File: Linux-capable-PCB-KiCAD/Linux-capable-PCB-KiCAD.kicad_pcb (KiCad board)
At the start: 4 copper layers, 167 parts, among them J1 UART_CONN, J2 GPIO_CONN, J3 USB_A, J4 USB_A, J5 Micro_SD_Card_Det, J6 MIC_DIFF_IN, J7 Barrel_Jack, U1 A33, U10 TPS62130, U11 AP131-25, U12 TPS62130, U13 TPS62130, U2 MMA8425Q_Gsensor, U3 SRV05-4, U4 MIPI_DSI_Raspberry, U5 SRV05-4, U6 SRV05-4, U7 ESP8089, U8 HTQ4G63AFR-PCB, U9 TPS62130, Y1 24MHz, Y2 32.768kHz, Y3 26 MHz

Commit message: clearence needs to be resolved
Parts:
- moved U8 42.0 mm to (172.7, 68.6), turned to 90 degrees
- moved U7 31.9 mm to (130.8, 54.6)
- moved J5 15.3 mm to (143.5, 50.8)
- moved U1 7.77 mm to (152.4, 78.7), turned to 180 degrees
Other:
- net class Outer_small added: clearance 0.1, trace_width 0.1, via_dia 0.4, via_drill 0.2
- net class Power added: clearance 0.2, trace_width 1, via_dia 0.8, via_drill 0.6
- rule trace_min: 0.2 -> 0.09
- rule via_min_drill: 0.3 -> 0.2

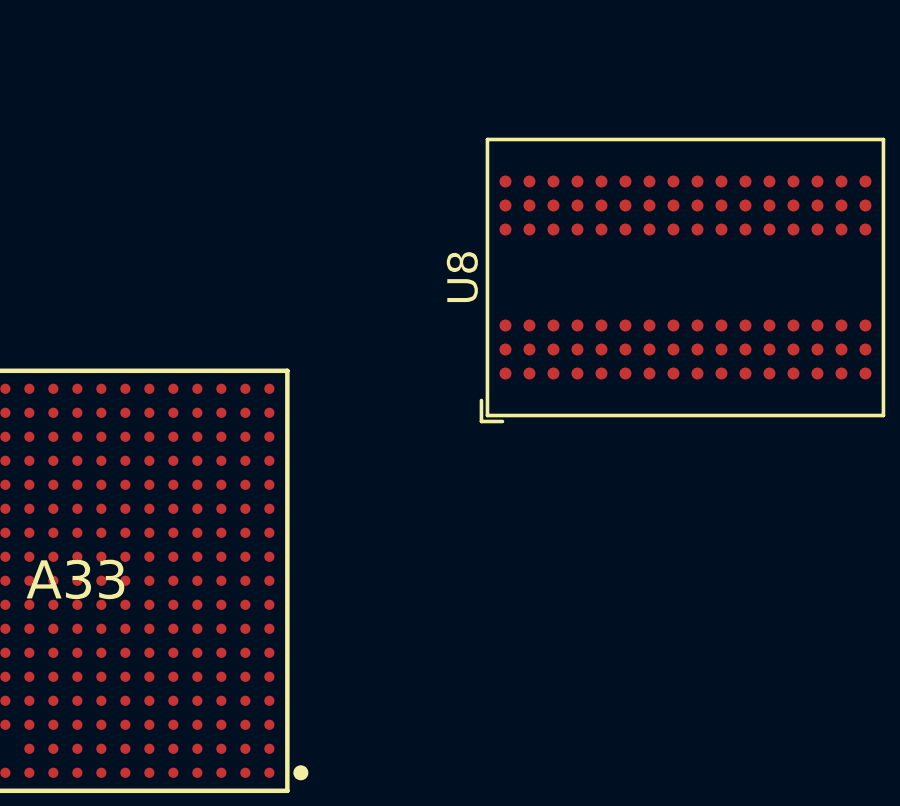
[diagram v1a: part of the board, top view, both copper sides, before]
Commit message: Some meandering lines added to RAM and processor links
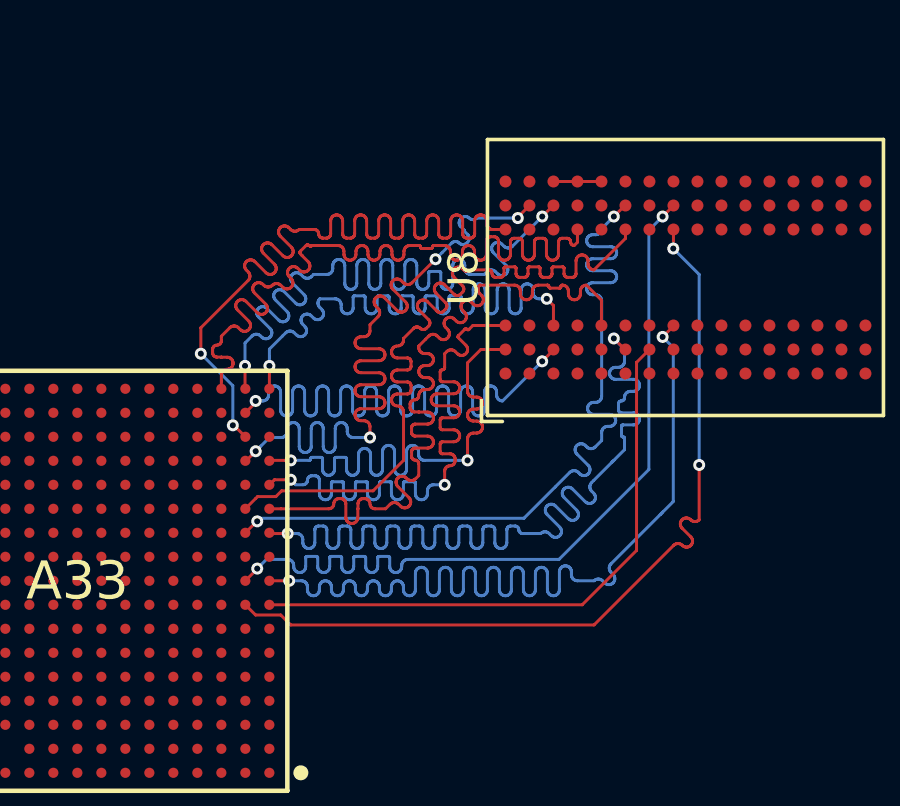
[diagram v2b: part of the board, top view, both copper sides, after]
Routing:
- net d2: track 0.00 -> 35.0 mm, vias 0 -> 2
- net d4: track 0.00 -> 34.9 mm, vias 0 -> 2
- net d5: track 0.00 -> 28.1 mm, vias 0 -> 2
- net d14: track 0.00 -> 28.1 mm, vias 0 -> 4
- net d0: track 0.00 -> 28.1 mm
- net d8: track 0.00 -> 28.0 mm
- net d12: track 0.00 -> 28.0 mm, vias 0 -> 2
- net d3: track 0.00 -> 28.0 mm, vias 0 -> 2
- net d7: track 0.00 -> 28.0 mm, vias 0 -> 2
- net d1: track 0.00 -> 27.9 mm
- net d10: track 0.00 -> 27.9 mm, vias 0 -> 2
- net d11: track 0.00 -> 26.7 mm, vias 0 -> 2
- net d9: track 0.00 -> 23.3 mm, vias 0 -> 2
- net d15: track 0.00 -> 23.1 mm, vias 0 -> 2
- net d6: track 0.00 -> 19.9 mm
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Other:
- net class Default: clearance 0.2 -> 0.12
- rule trace_clearance: 0.2 -> 0.12

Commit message: CPU and RAM
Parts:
- moved R3 81.3 mm to (170.4, 79.0)
- moved R4 76.6 mm to (170.4, 80.6)
- moved U8 1.74 mm to (172.4, 70.3)
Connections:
- net /RAM/CK renamed /RAM/CK_P
- net /RAM/~CK renamed /RAM/CK_N
- net Net-(R3-Pad1) renamed /DCK_P
- net Net-(R4-Pad1) renamed /DCK_N
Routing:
- net adr11: track 0.00 -> 58.9 mm, vias 0 -> 2
- net adr7: track 0.00 -> 56.0 mm, vias 0 -> 2
- net adr4: track 0.00 -> 55.8 mm, vias 0 -> 2
- net adr2: track 0.00 -> 45.0 mm, vias 0 -> 2
- net adr6: track 0.00 -> 44.4 mm
- net adr9: track 0.00 -> 44.3 mm, vias 0 -> 2
- net adr13: track 0.00 -> 44.3 mm, vias 0 -> 2
- net adr12: track 0.00 -> 44.3 mm
- net adr1: track 0.00 -> 44.3 mm
- net adr14: track 0.00 -> 44.3 mm
- net adr8: track 0.00 -> 44.3 mm
- net adr3: track 0.00 -> 43.9 mm, vias 0 -> 2
- net adr10: track 0.00 -> 43.9 mm, vias 0 -> 2
- net adr5: track 0.00 -> 43.6 mm
- net adr0: track 0.00 -> 43.3 mm, vias 0 -> 2
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
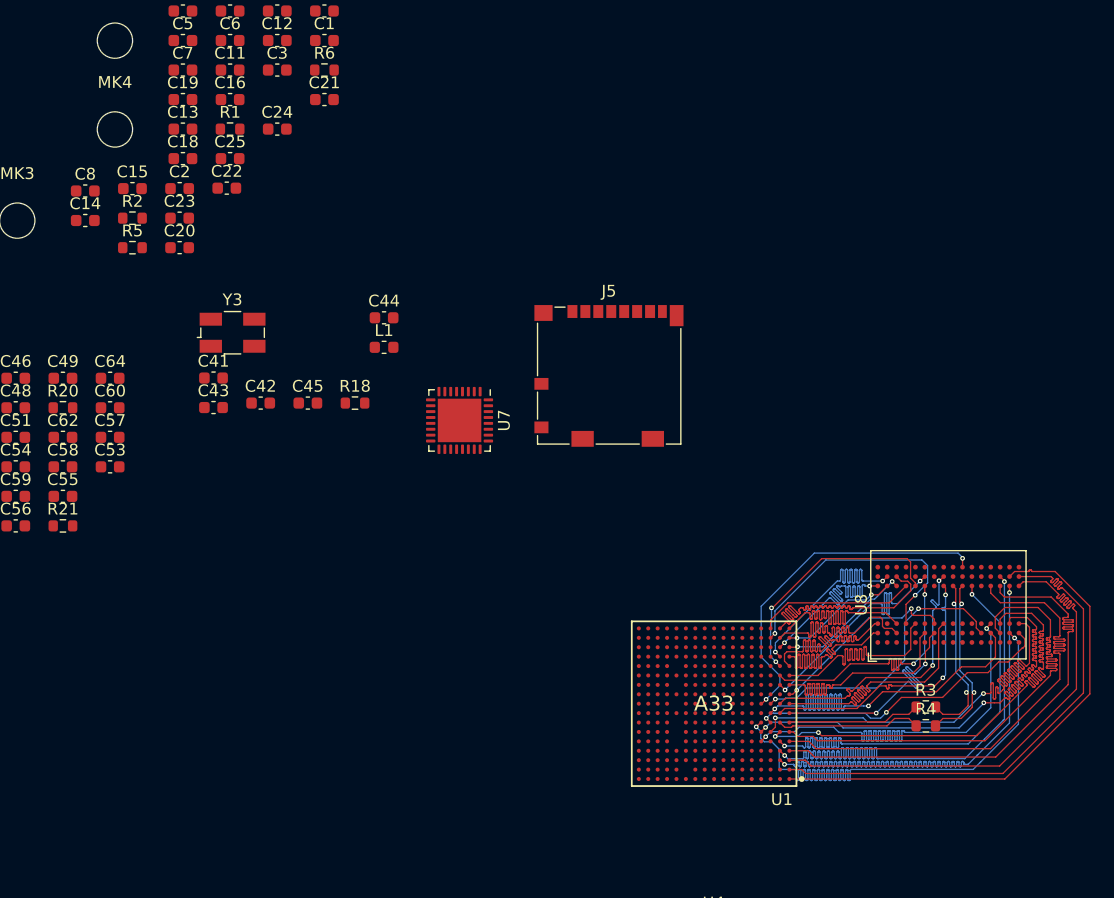
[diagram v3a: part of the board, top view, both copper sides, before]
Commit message: DDR3 - CPU layout
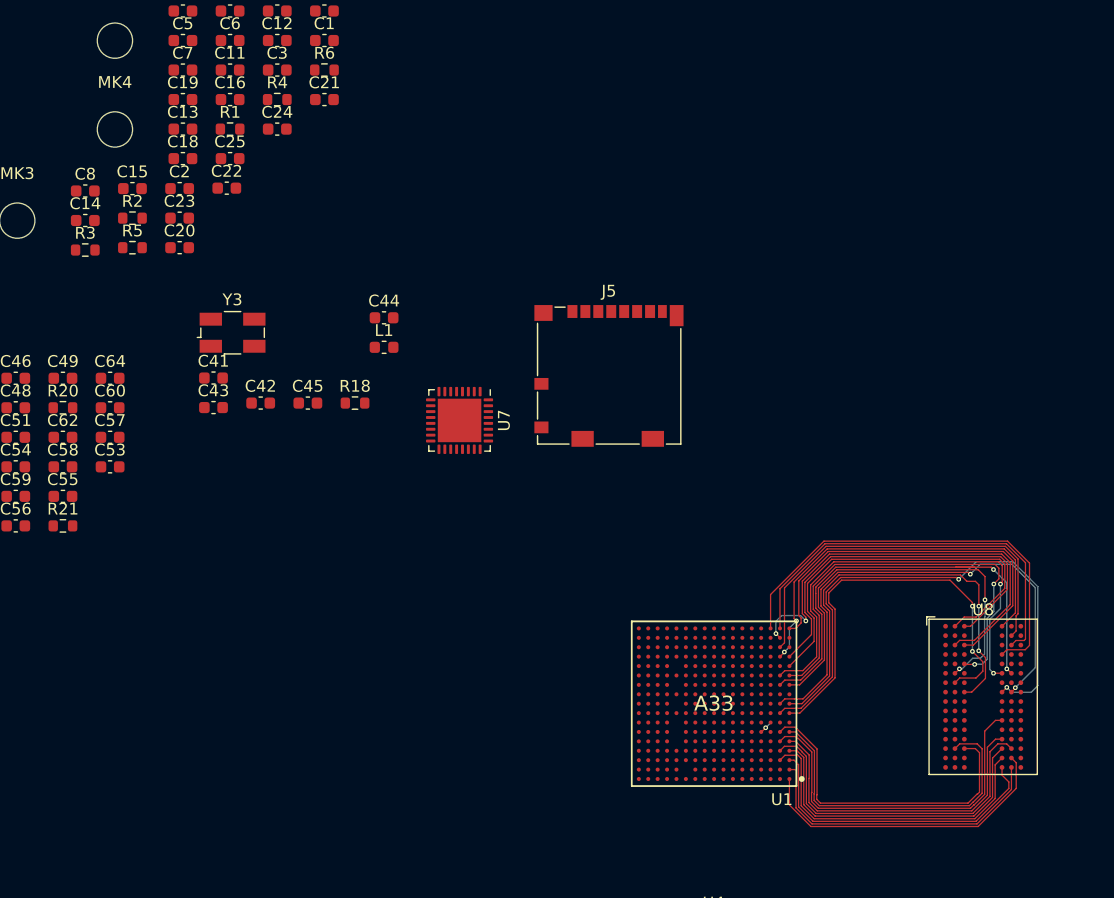
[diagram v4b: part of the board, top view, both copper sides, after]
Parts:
- moved R3 81.3 mm to (99.0, 40.1)
- moved R4 76.6 mm to (115.3, 27.3)
- moved U8 8.36 mm to (175.3, 78.1), turned to 0 degrees
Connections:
- U8 pad A2: d13 -> d15
- U8 pad A3: d15 -> d13
- U8 pad A7: d12 -> d14
- U8 pad B8: d14 -> d12
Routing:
- net adr7: track 56.0 -> 0.00 mm, vias 2 -> 0
- net adr13: track 44.3 -> 0.00 mm, vias 2 -> 0
- net adr3: track 43.9 -> 0.00 mm, vias 2 -> 0
- net adr0: track 43.3 -> 0.00 mm, vias 2 -> 0
- net adr9: track 44.3 -> 1.10 mm, vias 2 -> 1
- net adr11: track 58.9 -> 27.5 mm, vias 2 -> 0
- net /RAM/~CKE: track 29.6 -> 0.00 mm, vias 2 -> 0
- net /RAM/~RST: track 26.7 -> 0.00 mm, vias 2 -> 0
- net adr4: track 55.8 -> 29.4 mm, vias 2 -> 0
- net dba0: track 24.3 -> 0.00 mm, vias 2 -> 0
- net d8: track 13.4 -> 37.2 mm
- net /RAM/DMU: track 23.1 -> 0.00 mm, vias 2 -> 0
- net d7: track 24.0 -> 45.3 mm
- net /RAM/DML: track 21.2 -> 0.00 mm, vias 2 -> 0
- net adr8: track 44.3 -> 25.7 mm
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
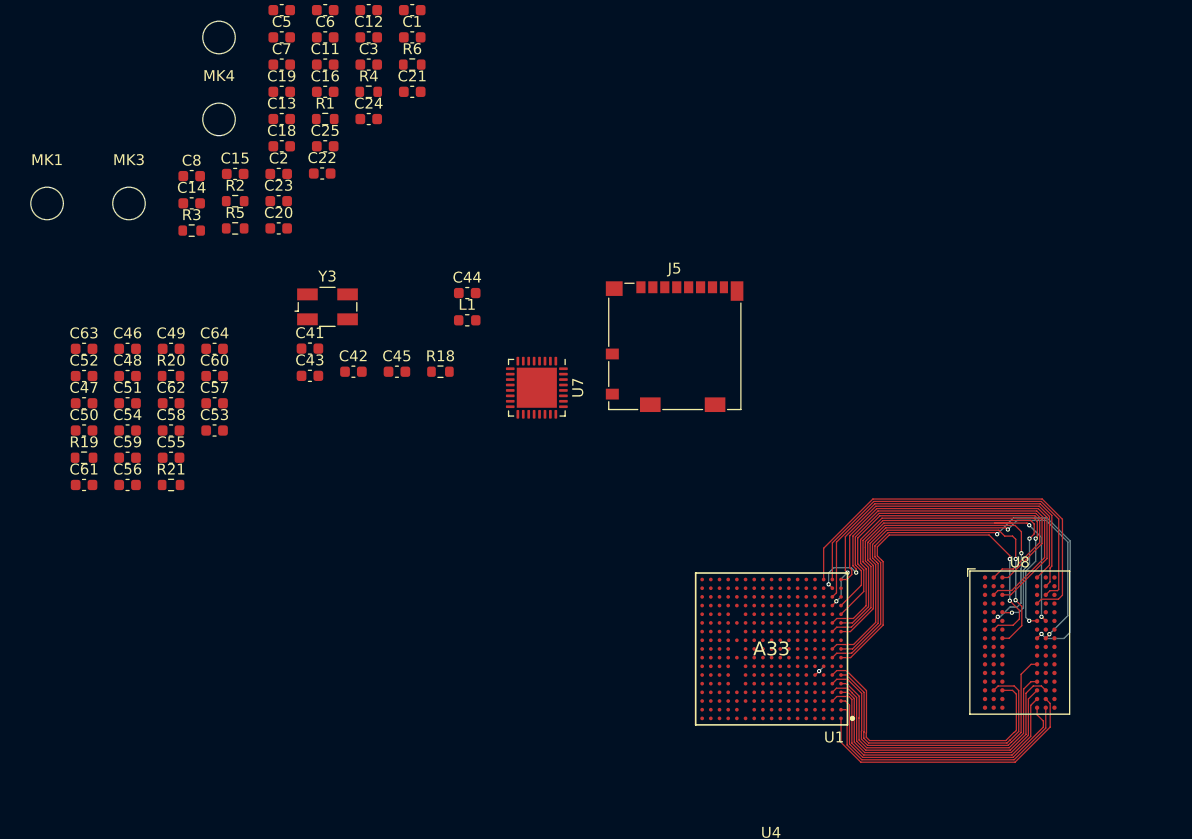
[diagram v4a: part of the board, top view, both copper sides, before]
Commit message: CPU and DDR3 connected
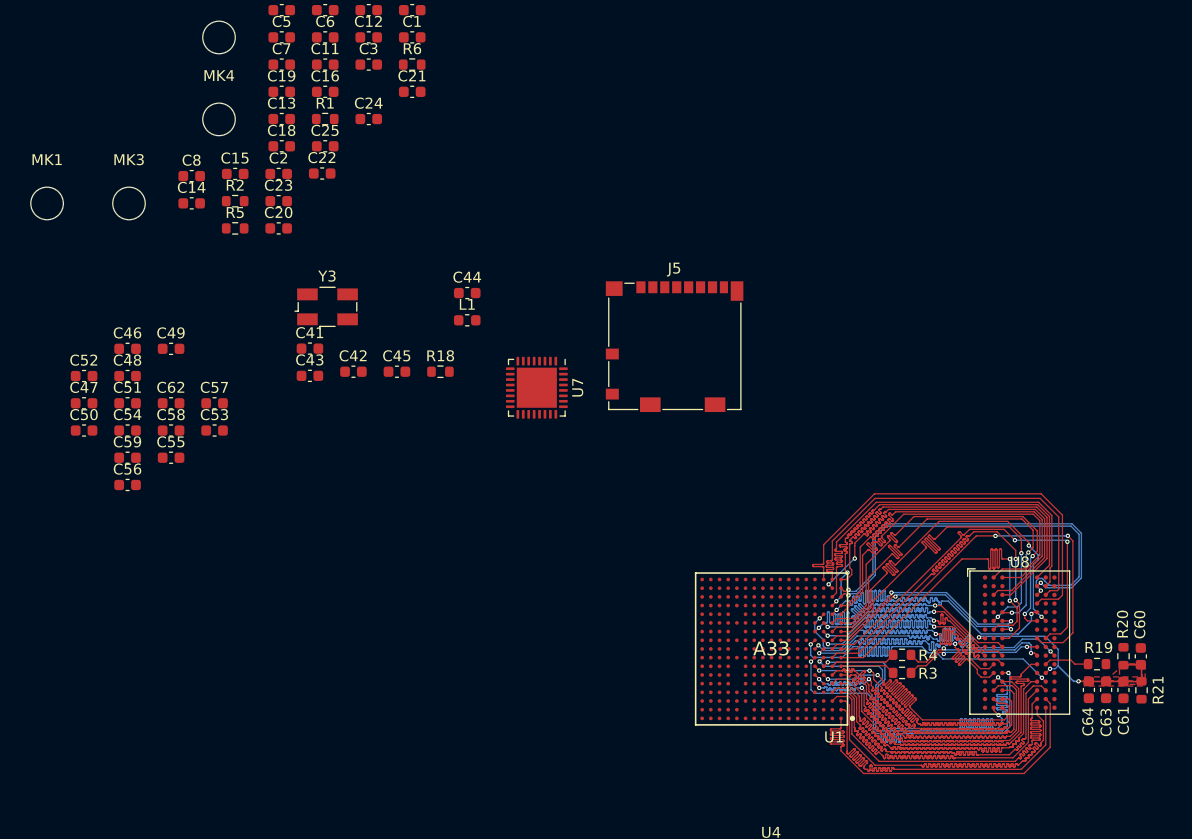
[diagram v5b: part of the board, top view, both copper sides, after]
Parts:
- moved C63 99.3 mm to (183.3, 82.5), turned to 270 degrees
- moved C61 97.7 mm to (184.9, 82.5), turned to 270 degrees
- moved R19 95.3 mm to (182.4, 80.1), turned to 180 degrees
- moved R20 91.5 mm to (184.9, 79.4), turned to 270 degrees
- moved R21 91.4 mm to (186.6, 82.5), turned to 270 degrees
- moved C60 89.2 mm to (186.5, 79.4), turned to 270 degrees
- moved C64 86.5 mm to (181.7, 82.5), turned to 270 degrees
- moved R3 77.1 mm to (164.5, 80.9)
- moved R4 71.5 mm to (164.5, 79.2)
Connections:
- net /RAM/DQSU renamed /DQS1_P
- net /RAM/~DQSL renamed /DQS0_N
- net /RAM/~DQSU renamed /DQS1_N
- C1 pad 1: +1V35 -> +1V5
- C46 pad 1: +1V35 -> +1V5
- C47 pad 1: +1V35 -> +1V5
- C48 pad 1: +1V35 -> +1V5
- C49 pad 1: +1V35 -> +1V5
- C51 pad 1: +1V35 -> +1V5
- C52 pad 1: +1V35 -> +1V5
- C54 pad 1: +1V35 -> +1V5
- C55 pad 1: +1V35 -> +1V5
- C56 pad 1: +1V35 -> +1V5
- C57 pad 1: +1V35 -> +1V5
- C58 pad 1: +1V35 -> +1V5
- C59 pad 1: +1V35 -> +1V5
- C60 pad 1: +1V35 -> +1V5
- C62 pad 1: +1V35 -> +1V5
- R1 pad 1: +1V35 -> +1V5
- R20 pad 1: +1V35 -> +1V5
- R38 pad 1: +1V35 -> +1V5
- U1 pad K2: /RAM/DQSL -> /DQS0_P
- U8 pad A1: +1V35 -> +1V5
- U8 pad A8: +1V35 -> +1V5
- U8 pad B2: +1V35 -> +1V5
- U8 pad C1: +1V35 -> +1V5
- U8 pad C9: +1V35 -> +1V5
- U8 pad D2: +1V35 -> +1V5
- U8 pad D9: +1V35 -> +1V5
- U8 pad E9: +1V35 -> +1V5
- U8 pad F1: +1V35 -> +1V5
- U8 pad F3: (no net) -> /DQS0_P
- U8 pad G7: +1V35 -> +1V5
- U8 pad H2: +1V35 -> +1V5
- U8 pad H9: +1V35 -> +1V5
- U8 pad K2: +1V35 -> +1V5
- U8 pad K8: +1V35 -> +1V5
- U8 pad N1: +1V35 -> +1V5
- U8 pad N9: +1V35 -> +1V5
- U8 pad R1: +1V35 -> +1V5
- U8 pad R9: +1V35 -> +1V5
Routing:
- net /RAM/DML: track 0.00 -> 41.0 mm, vias 0 -> 2
- net dba0: track 0.00 -> 38.1 mm, vias 0 -> 2
- net /RAM/~CKE: track 0.00 -> 38.0 mm, vias 0 -> 2
- net /RAM/~WE: track 0.00 -> 38.0 mm, vias 0 -> 2
- net /RAM/~RAS: track 0.00 -> 38.0 mm, vias 0 -> 2
- net adr7: track 0.00 -> 38.0 mm, vias 0 -> 2
- net /RAM/~CS: track 0.00 -> 38.0 mm, vias 0 -> 2
- net /RAM/~RST: track 0.00 -> 38.0 mm, vias 0 -> 2
- net dba1: track 0.00 -> 38.0 mm, vias 0 -> 2
- net adr13: track 0.00 -> 38.0 mm, vias 0 -> 2
- net dba2: track 0.00 -> 38.0 mm, vias 0 -> 2
- net adr3: track 0.00 -> 38.0 mm, vias 0 -> 2
- net adr0: track 0.00 -> 37.7 mm, vias 0 -> 2
- net /DQS1_P: track 0.00 -> 37.3 mm, vias 0 -> 2
- net /DQS1_N: track 0.00 -> 36.3 mm, vias 0 -> 2
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- added copper zone on F.Cu, net Net-(C60-Pad2)

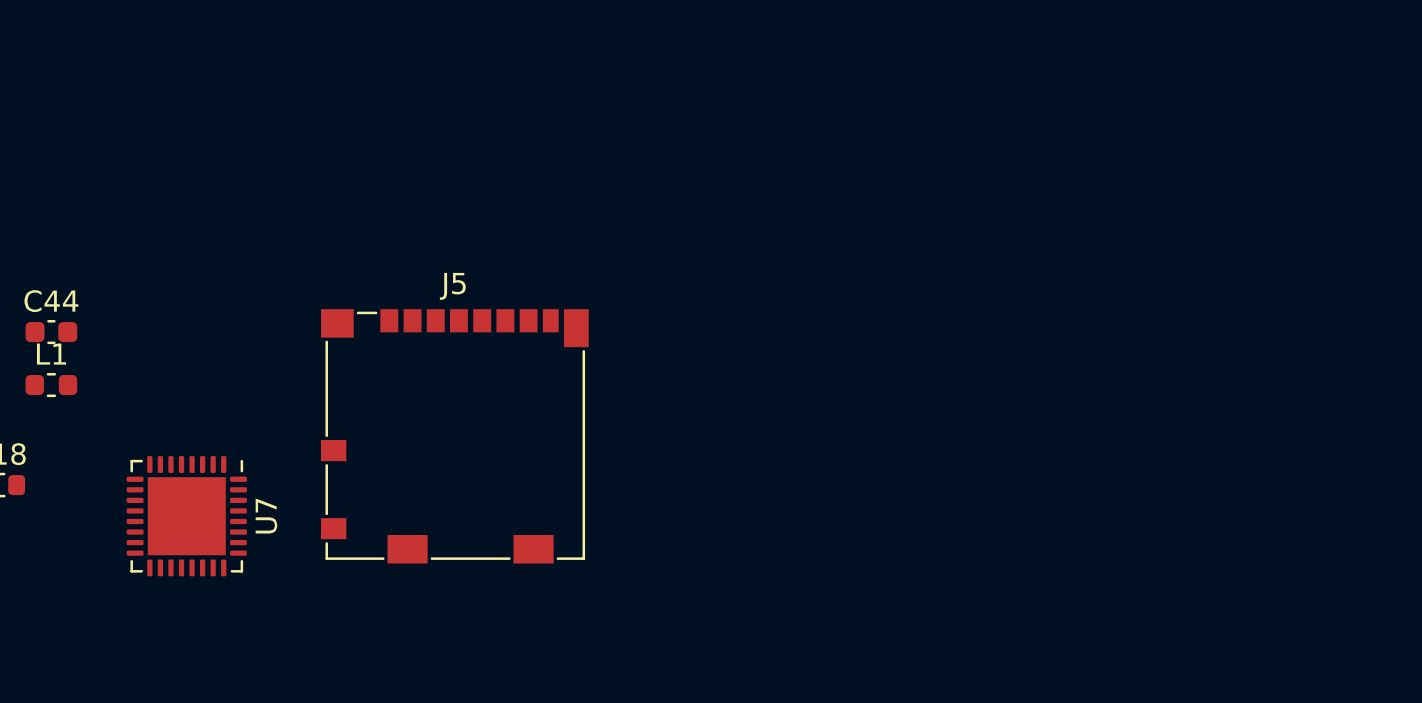
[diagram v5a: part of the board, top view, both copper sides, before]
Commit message: Added an antenna
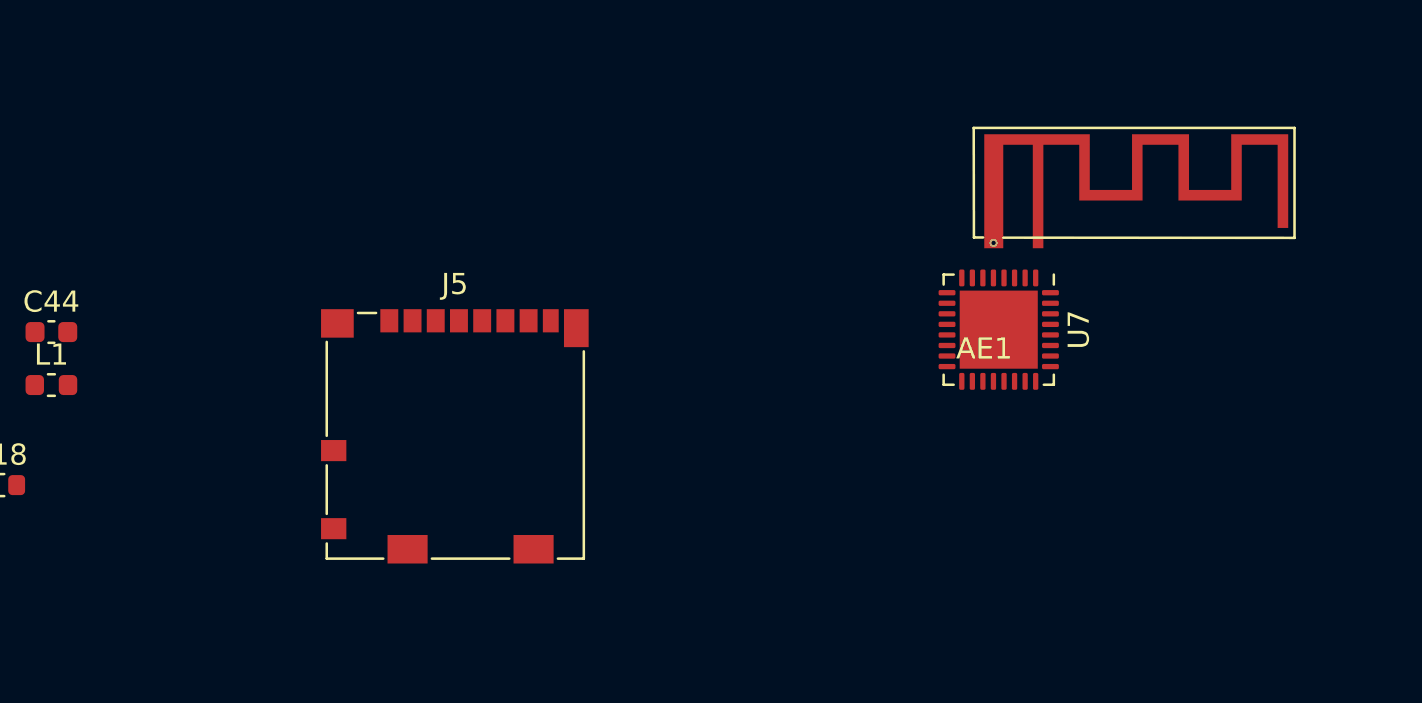
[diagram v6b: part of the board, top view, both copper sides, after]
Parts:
- added AE1: Antenna_Dipole, Small2_4GHz_PCB_Antenna:Small2_4GHz_PCB_Antenna, F.Cu at (168.6, 36.5)
- moved U7 39.5 mm to (169.3, 45.8)
